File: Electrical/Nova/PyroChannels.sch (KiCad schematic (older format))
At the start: 5 parts, among them J4 Conn_01x02_Female, J5 Conn_01x04_Female, J6 Conn_01x04_Female

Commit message: Misc Changes
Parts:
- J5, J6: Order Link (none) -> https://www.digikey.com/en/products/detail/phoenix-contact/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
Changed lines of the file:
@@
 $Descr USLetter 11000 8500
 encoding utf-8
-Sheet 10 20
+Sheet 9 20
 Title ""
 Date ""
@@
 F 1 "Conn_01x04_Female" H 8028 3785 50  0000 L CNN
 F 2 "" H 8000 3900 50  0001 C CNN
-F 3 "~" H 8000 3900 50  0001 C CNN
+F 3 "" H 8000 3900 50  0001 C CNN
+F 4 "https://www.digikey.com/en/products/detail/phoenix-contact/1770908/2192462" H 8000 3900 50  0001 C CNN "Order Link"
 	1    8000 3900
 	1    0    0    -1
@@
 F 2 "" H 8000 4600 50  0001 C CNN
 F 3 "~" H 8000 4600 50  0001 C CNN
+F 4 "https://www.digikey.com/en/products/detail/phoenix-contact/1770908/2192462" H 8000 4600 50  0001 C CNN "Order Link"
 	1    8000 4600
 	1    0    0    -1

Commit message: Finished adding footprints
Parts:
- J4: footprint (none) -> TerminalBlock_Phoenix:TerminalBlock_Phoenix_PTSM-0,5-2-2.5-H-THR_1x02_P2.50mm_Horizontal; Order Link (none) -> https://www.digikey.com/en/products/detail/phoenix-contact/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
- J5, J6: footprint (none) -> TerminalBlock_Phoenix:TerminalBlock_Phoenix_PTSM-0,5-4-2.5-H-THR_1x04_P2.50mm_Horizontal
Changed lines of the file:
@@
 F 0 "J5" H 8028 3876 50  0000 L CNN
 F 1 "Conn_01x04_Female" H 8028 3785 50  0000 L CNN
-F 2 "" H 8000 3900 50  0001 C CNN
+F 2 "TerminalBlock_Phoenix:TerminalBlock_Phoenix_PTSM-0,5-4-2.5-H-THR_1x04_P2.50mm_Horizontal" H 8000 3900 50  0001 C CNN
 F 3 "" H 8000 3900 50  0001 C CNN
 F 4 "https://www.digikey.com/en/products/detail/phoenix-contact/1770908/2192462" H 8000 3900 50  0001 C CNN "Order Link"
@@
 F 0 "J6" H 8028 4576 50  0000 L CNN
 F 1 "Conn_01x04_Female" H 8028 4485 50  0000 L CNN
-F 2 "" H 8000 4600 50  0001 C CNN
+F 2 "TerminalBlock_Phoenix:TerminalBlock_Phoenix_PTSM-0,5-4-2.5-H-THR_1x04_P2.50mm_Horizontal" H 8000 4600 50  0001 C CNN
 F 3 "~" H 8000 4600 50  0001 C CNN
 F 4 "https://www.digikey.com/en/products/detail/phoenix-contact/1770908/2192462" H 8000 4600 50  0001 C CNN "Order Link"
@@
 F 0 "J4" H 2978 2526 50  0000 L CNN
 F 1 "Conn_01x02_Female" H 2978 2435 50  0000 L CNN
-F 2 "" H 2950 2550 50  0001 C CNN
+F 2 "TerminalBlock_Phoenix:TerminalBlock_Phoenix_PTSM-0,5-2-2.5-H-THR_1x02_P2.50mm_Horizontal" H 2950 2550 50  0001 C CNN
 F 3 "~" H 2950 2550 50  0001 C CNN
+F 4 "https://www.digikey.com/en/products/detail/phoenix-contact/1770885/2192460" H 2950 2550 50  0001 C CNN "Order Link"
 	1    2950 2550
 	1    0    0    -1

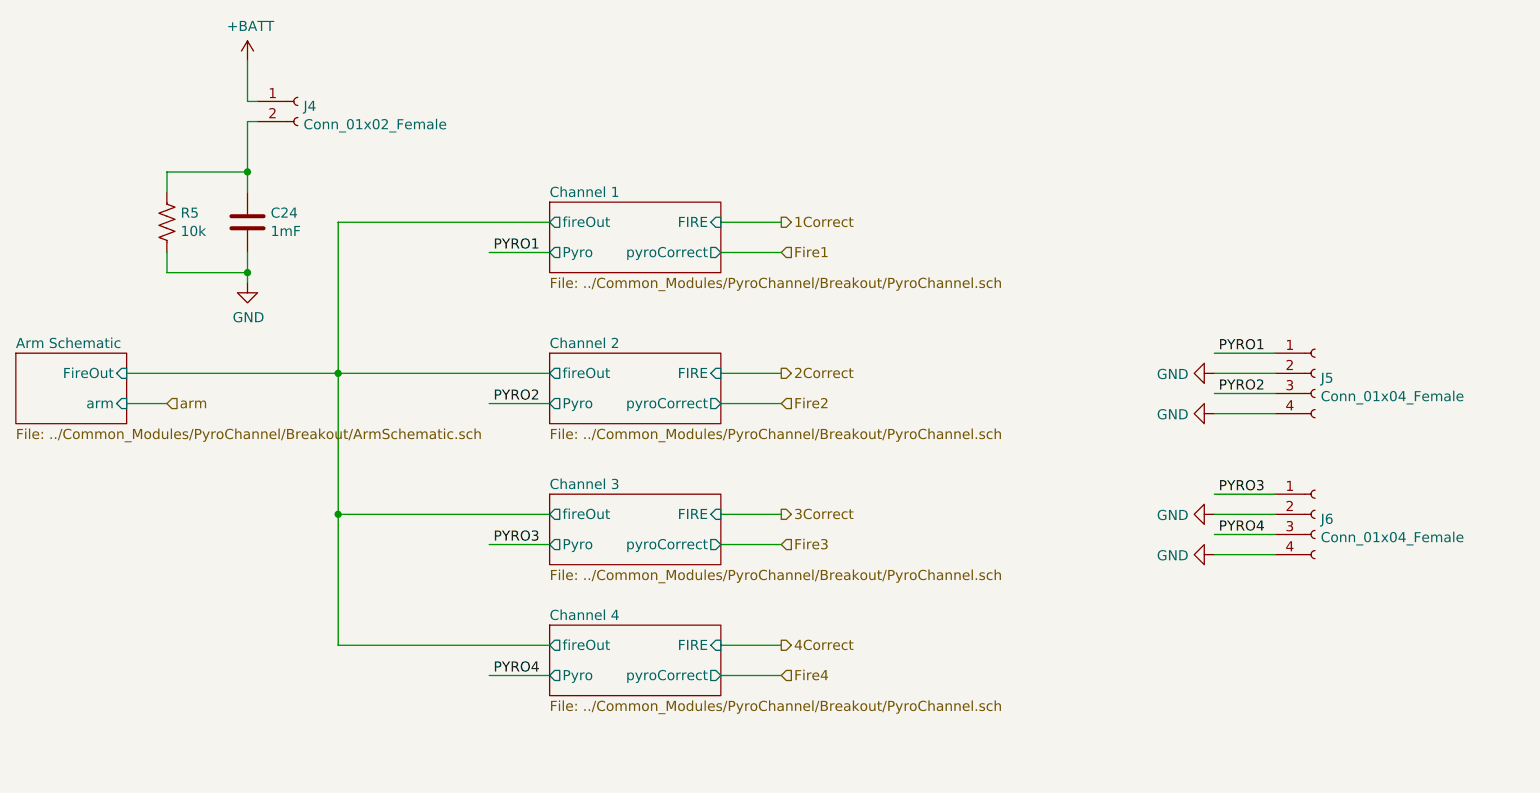
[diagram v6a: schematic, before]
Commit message: Began Laying out sub modules
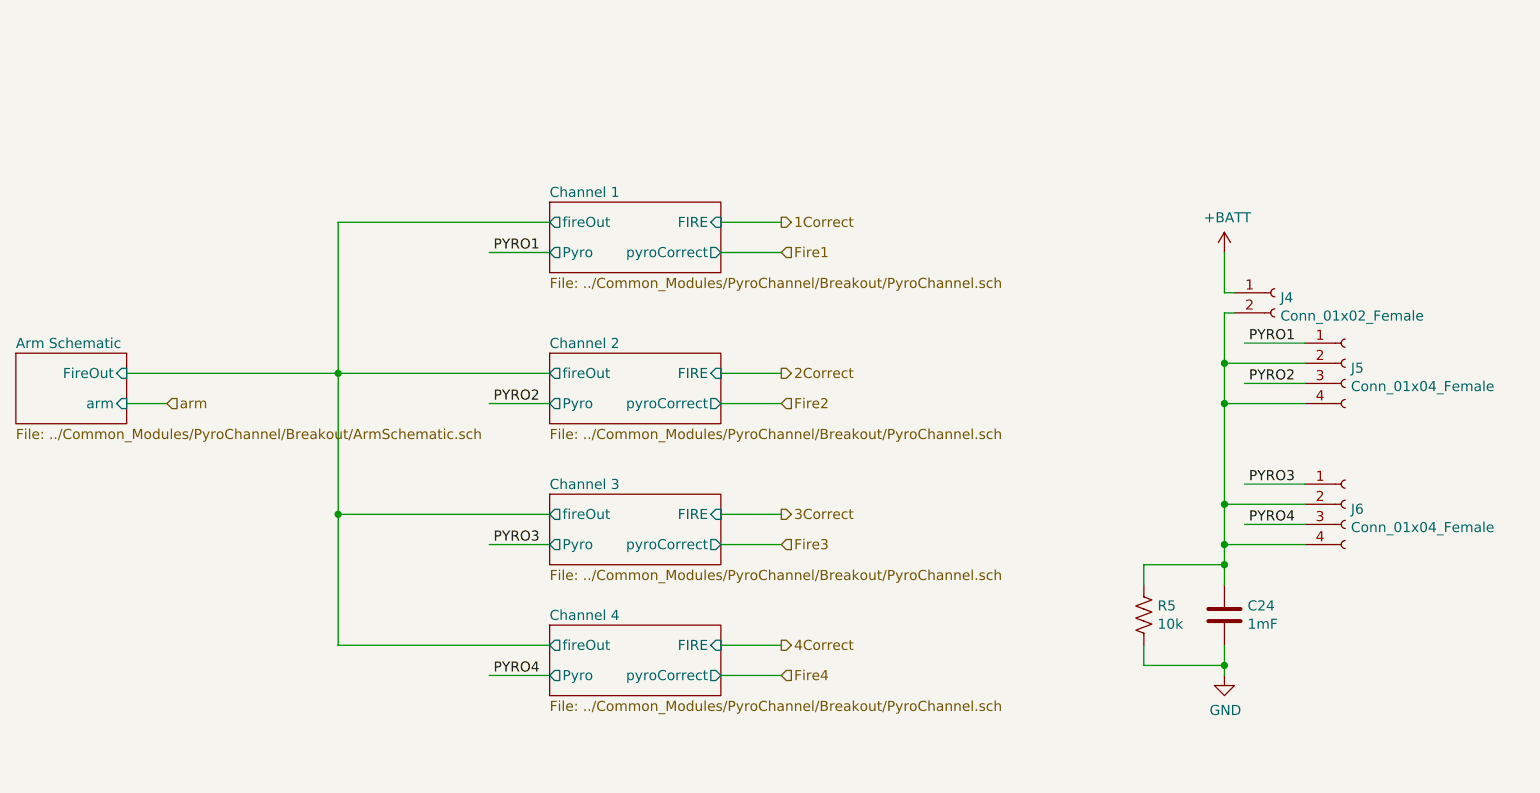
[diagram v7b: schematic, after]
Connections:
- wire segments 40 -> 44
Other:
- moved on the sheet: C24, J4, J5, J6, R5
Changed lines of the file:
@@
 L Device:C C24
 U 1 1 5F4497A2
-P 2700 3150
-F 0 "C24" H 2815 3196 50  0000 L CNN
-F 1 "1mF" H 2815 3105 50  0000 L CNN
-F 2 "PyroChannel:CP_Radial_D10.0mm_P5.00mm" H 2738 3000 50  0001 C CNN
-F 3 "~" H 2700 3150 50  0001 C CNN
-F 4 "1189-3703-1-ND" H 2700 3150 50  0001 C CNN "digikey"
-	1    2700 3150
+P 7550 5100
+F 0 "C24" H 7665 5146 50  0000 L CNN
+F 1 "1mF" H 7665 5055 50  0000 L CNN
+F 2 "PyroChannel:CP_Radial_D10.0mm_P5.00mm" H 7588 4950 50  0001 C CNN
+F 3 "~" H 7550 5100 50  0001 C CNN
+F 4 "1189-3703-1-ND" H 7550 5100 50  0001 C CNN "digikey"
+	1    7550 5100
 	1    0    0    -1
 $EndComp
@@
 L power:+BATT #PWR035
 U 1 1 5F449DDB
-P 2700 2350
-F 0 "#PWR035" H 2700 2200 50  0001 C CNN
-F 1 "+BATT" H 2715 2523 50  0000 C CNN
-F 2 "" H 2700 2350 50  0001 C CNN
-F 3 "" H 2700 2350 50  0001 C CNN
-	1    2700 2350
+P 7550 3300
+F 0 "#PWR035" H 7550 3150 50  0001 C CNN
+F 1 "+BATT" H 7565 3473 50  0000 C CNN
+F 2 "" H 7550 3300 50  0001 C CNN
+F 3 "" H 7550 3300 50  0001 C CNN
+	1    7550 3300
 	1    0    0    -1
 $EndComp
@@
 L power:GND #PWR036
 U 1 1 5F44A4A7
-P 2700 3450
-F 0 "#PWR036" H 2700 3200 50  0001 C CNN
-F 1 "GND" H 2705 3277 50  0000 C CNN
-F 2 "" H 2700 3450 50  0001 C CNN
-F 3 "" H 2700 3450 50  0001 C CNN
-	1    2700 3450
-	1    0    0    -1
-$EndComp
-Wire Wire Line
-	2700 3300 2700 3400
-Wire Wire Line
-	2300 3300 2300 3400
-Wire Wire Line
-	2300 3400 2700 3400
-Connection ~ 2700 3400
-Wire Wire Line
-	2700 3400 2700 3450
-Wire Wire Line
-	2300 3000 2300 2900
-Wire Wire Line
-	2300 2900 2700 2900
-Connection ~ 2700 2900
-Wire Wire Line
-	2700 2900 2700 3000
+P 7550 5400
+F 0 "#PWR036" H 7550 5150 50  0001 C CNN
+F 1 "GND" H 7555 5227 50  0000 C CNN
+F 2 "" H 7550 5400 50  0001 C CNN
+F 3 "" H 7550 5400 50  0001 C CNN
+	1    7550 5400
+	1    0    0    -1
+$EndComp
+Wire Wire Line
+	7550 5250 7550 5350
+Wire Wire Line
+	7150 5250 7150 5350
+Wire Wire Line
+	7150 5350 7550 5350
+Connection ~ 7550 5350
+Wire Wire Line
+	7550 5350 7550 5400
+Wire Wire Line
+	7150 4950 7150 4850
+Wire Wire Line
+	7150 4850 7550 4850
+Wire Wire Line
+	7550 4850 7550 4950
 $Comp
 L Device:R_US R5
 U 1 1 5F6ECA83
-P 2300 3150
-F 0 "R5" H 2368 3196 50  0000 L CNN
-F 1 "10k" H 2368 3105 50  0000 L CNN
-F 2 "Resistor_SMD:R_0402_1005Metric" V 2340 3140 50  0001 C CNN
-F 3 "~" H 2300 3150 50  0001 C CNN
-	1    2300 3150
+P 7150 5100
+F 0 "R5" H 7218 5146 50  0000 L CNN
+F 1 "10k" H 7218 5055 50  0000 L CNN
+F 2 "Resistor_SMD:R_0402_1005Metric" V 7190 5090 50  0001 C CNN
+F 3 "~" H 7150 5100 50  0001 C CNN
+	1    7150 5100
 	1    0    0    -1
 $EndComp
@@
 L Connector:Conn_01x04_Female J5
 U 1 1 6033E472
-P 8000 3900
-F 0 "J5" H 8028 3876 50  0000 L CNN
-F 1 "Conn_01x04_Female" H 8028 3785 50  0000 L CNN
-F 2 "TerminalBlock_Phoenix:TerminalBlock_Phoenix_PTSM-0,5-4-2.5-H-THR_1x04_P2.50mm_Horizontal" H 8000 3900 50  0001 C CNN
-F 3 "" H 8000 3900 50  0001 C CNN
-F 4 "https://www.digikey.com/en/products/detail/phoenix-contact/1770908/2192462" H 8000 3900 50  0001 C CNN "Order Link"
-	1    8000 3900
+P 8150 3850
+F 0 "J5" H 8178 3826 50  0000 L CNN
+F 1 "Conn_01x04_Female" H 8178 3735 50  0000 L CNN
+F 2 "TerminalBlock_Phoenix:TerminalBlock_Phoenix_PTSM-0,5-4-2.5-H-THR_1x04_P2.50mm_Horizontal" H 8150 3850 50  0001 C CNN
+F 3 "" H 8150 3850 50  0001 C CNN
+F 4 "https://www.digikey.com/en/products/detail/phoenix-contact/1770908/2192462" H 8150 3850 50  0001 C CNN "Order Link"
+	1    8150 3850
 	1    0    0    -1
 $EndComp
@@
 L Connector:Conn_01x04_Female J6
 U 1 1 6033EDCD
-P 8000 4600
-F 0 "J6" H 8028 4576 50  0000 L CNN
-F 1 "Conn_01x04_Female" H 8028 4485 50  0000 L CNN
-F 2 "TerminalBlock_Phoenix:TerminalBlock_Phoenix_PTSM-0,5-4-2.5-H-THR_1x04_P2.50mm_Horizontal" H 8000 4600 50  0001 C CNN
-F 3 "~" H 8000 4600 50  0001 C CNN
-F 4 "https://www.digikey.com/en/products/detail/phoenix-contact/1770908/2192462" H 8000 4600 50  0001 C CNN "Order Link"
-	1    8000 4600
-	1    0    0    -1
-$EndComp
-Wire Wire Line
-	7800 3800 7500 3800
-Text Label 7750 3800 2    50   ~ 0
+P 8150 4550
+F 0 "J6" H 8178 4526 50  0000 L CNN
+F 1 "Conn_01x04_Female" H 8178 4435 50  0000 L CNN
+F 2 "TerminalBlock_Phoenix:TerminalBlock_Phoenix_PTSM-0,5-4-2.5-H-THR_1x04_P2.50mm_Horizontal" H 8150 4550 50  0001 C CNN
+F 3 "~" H 8150 4550 50  0001 C CNN
+F 4 "https://www.digikey.com/en/products/detail/phoenix-contact/1770908/2192462" H 8150 4550 50  0001 C CNN "Order Link"
+	1    8150 4550
+	1    0    0    -1
+$EndComp
+Wire Wire Line
+	7950 3750 7650 3750
+Text Label 7900 3750 2    50   ~ 0
 PYRO1
 Wire Wire Line
-	7800 4000 7500 4000
-Text Label 7750 4000 2    50   ~ 0
+	7950 3950 7650 3950
+Text Label 7900 3950 2    50   ~ 0
 PYRO2
 Wire Wire Line
-	7800 4500 7500 4500
-Text Label 7750 4500 2    50   ~ 0
+	7950 4450 7650 4450
+Text Label 7900 4450 2    50   ~ 0
 PYRO3
 Wire Wire Line
-	7800 4700 7500 4700
-Text Label 7750 4700 2    50   ~ 0
+	7950 4650 7650 4650
+Text Label 7900 4650 2    50   ~ 0
 PYRO4
-$Comp
-L power:GND #PWR0128
-U 1 1 60342F05
-P 7500 3900
-F 0 "#PWR0128" H 7500 3650 50  0001 C CNN
-F 1 "GND" V 7505 3772 50  0000 R CNN
-F 2 "" H 7500 3900 50  0001 C CNN
-F 3 "" H 7500 3900 50  0001 C CNN
-	1    7500 3900
-	0    1    1    0
-$EndComp
-$Comp
-L power:GND #PWR0129
-U 1 1 603438C3
-P 7500 4100
-F 0 "#PWR0129" H 7500 3850 50  0001 C CNN
-F 1 "GND" V 7505 3972 50  0000 R CNN
-F 2 "" H 7500 4100 50  0001 C CNN
-F 3 "" H 7500 4100 50  0001 C CNN
-	1    7500 4100
-	0    1    1    0
-$EndComp
-$Comp
-L power:GND #PWR0130
-U 1 1 60343E90
-P 7500 4600
-F 0 "#PWR0130" H 7500 4350 50  0001 C CNN
-F 1 "GND" V 7505 4472 50  0000 R CNN
-F 2 "" H 7500 4600 50  0001 C CNN
-F 3 "" H 7500 4600 50  0001 C CNN
-	1    7500 4600
-	0    1    1    0
-$EndComp
-$Comp
-L power:GND #PWR0131
-U 1 1 603444B0
-P 7500 4800
-F 0 "#PWR0131" H 7500 4550 50  0001 C CNN
-F 1 "GND" V 7505 4672 50  0000 R CNN
-F 2 "" H 7500 4800 50  0001 C CNN
-F 3 "" H 7500 4800 50  0001 C CNN
-	1    7500 4800
-	0    1    1    0
-$EndComp
-Wire Wire Line
-	7800 4800 7500 4800
-Wire Wire Line
-	7500 4600 7800 4600
-Wire Wire Line
-	7800 4100 7500 4100
-Wire Wire Line
-	7500 3900 7800 3900
 $Comp
 L Connector:Conn_01x02_Female J4
 U 1 1 60348F4E
-P 2950 2550
-F 0 "J4" H 2978 2526 50  0000 L CNN
-F 1 "Conn_01x02_Female" H 2978 2435 50  0000 L CNN
-F 2 "TerminalBlock_Phoenix:TerminalBlock_Phoenix_PTSM-0,5-2-2.5-H-THR_1x02_P2.50mm_Horizontal" H 2950 2550 50  0001 C CNN
-F 3 "~" H 2950 2550 50  0001 C CNN
-F 4 "https://www.digikey.com/en/products/detail/phoenix-contact/1770885/2192460" H 2950 2550 50  0001 C CNN "Order Link"
-	1    2950 2550
-	1    0    0    -1
-$EndComp
-Wire Wire Line
-	2700 2350 2700 2550
-Wire Wire Line
-	2700 2550 2750 2550
-Wire Wire Line
-	2750 2650 2700 2650
-Wire Wire Line
-	2700 2650 2700 2900
+P 7800 3500
+F 0 "J4" H 7828 3476 50  0000 L CNN
+F 1 "Conn_01x02_Female" H 7828 3385 50  0000 L CNN
+F 2 "TerminalBlock_Phoenix:TerminalBlock_Phoenix_PTSM-0,5-2-2.5-H-THR_1x02_P2.50mm_Horizontal" H 7800 3500 50  0001 C CNN
+F 3 "~" H 7800 3500 50  0001 C CNN
+F 4 "https://www.digikey.com/en/products/detail/phoenix-contact/1770885/2192460" H 7800 3500 50  0001 C CNN "Order Link"
+	1    7800 3500
+	1    0    0    -1
+$EndComp
+Wire Wire Line
+	7550 3300 7550 3500
+Wire Wire Line
+	7550 3500 7600 3500
+Wire Wire Line
+	7600 3600 7550 3600
+Wire Wire Line
+	7550 3600 7550 3850
+Wire Wire Line
+	7550 4850 7550 4750
+Wire Wire Line
+	7550 4750 7950 4750
+Connection ~ 7550 4850
+Wire Wire Line
+	7550 4750 7550 4550
+Wire Wire Line
+	7550 4550 7950 4550
+Connection ~ 7550 4750
+Wire Wire Line
+	7550 4050 7950 4050
+Wire Wire Line
+	7550 4050 7550 4550
+Connection ~ 7550 4550
+Wire Wire Line
+	7550 3850 7550 4050
+Wire Wire Line
+	7550 3850 7950 3850
+Connection ~ 7550 4050
+Connection ~ 7550 3850
 $EndSCHEMATC

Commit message: More Layout
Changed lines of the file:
@@
 Wire Wire Line
 	7950 3750 7650 3750
-Text Label 7900 3750 2    50   ~ 0
+Text Label 7900 3950 2    50   ~ 0
 PYRO1
 Wire Wire Line
 	7950 3950 7650 3950
-Text Label 7900 3950 2    50   ~ 0
+Text Label 7900 3750 2    50   ~ 0
 PYRO2
 Wire Wire Line
 	7950 4450 7650 4450
-Text Label 7900 4450 2    50   ~ 0
+Text Label 7900 4650 2    50   ~ 0
 PYRO3
 Wire Wire Line
 	7950 4650 7650 4650
-Text Label 7900 4650 2    50   ~ 0
+Text Label 7900 4450 2    50   ~ 0
 PYRO4
 $Comp
